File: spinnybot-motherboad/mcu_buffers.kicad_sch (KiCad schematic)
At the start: 14 parts, among them Q3 BC846, U2 XBP9B-DMWTB002, U3 MC14504BDR2G, U5 ESP32-DEVKITC-32D, U7 SN74AHCT541DW

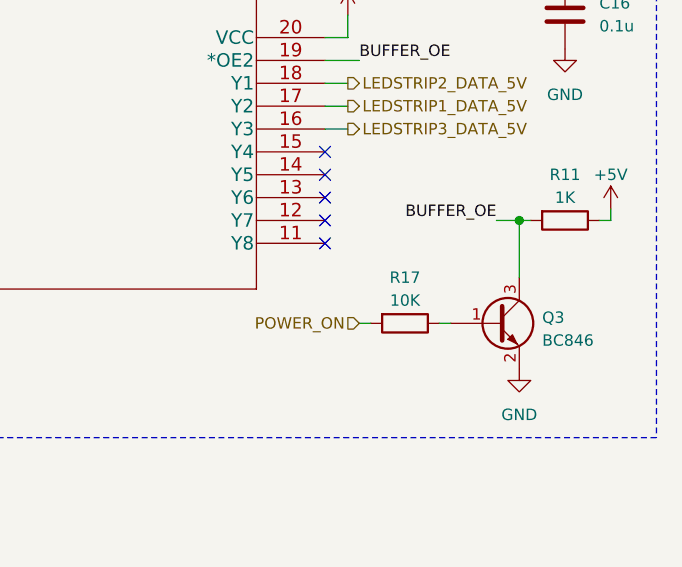
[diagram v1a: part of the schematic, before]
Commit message: Updated voltage divider on power circuit
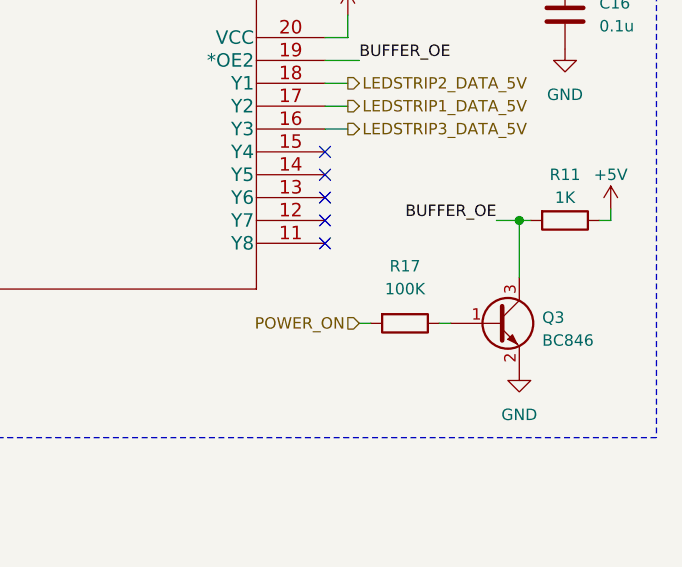
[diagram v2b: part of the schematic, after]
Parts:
- R17: value 10K -> 100K
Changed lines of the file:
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@@
   (symbol (lib_id "Device:R") (at 254 105.41 270) (unit 1)
     (in_bom yes) (on_board yes) (fields_autoplaced)
-    (property "Reference" "R17" (id 0) (at 254 100.33 90))
-    (property "Value" "10K" (id 1) (at 254 102.87 90))
+    (property "Reference" "R17" (id 0) (at 254 99.06 90))
+    (property "Value" "100K" (id 1) (at 254 101.6 90))
     (property "Footprint" "Resistor_SMD:R_0805_2012Metric_Pad1.20x1.40mm_HandSolder" (id 2) (at 254 103.632 90)
       (effects (font (size 1.27 1.27)) hide)
